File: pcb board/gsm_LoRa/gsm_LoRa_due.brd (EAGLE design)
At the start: 71.4 x 51.2 mm, 42 parts, among them IC1 TPS22810TDBVRQ1, IC2 TPS22810TDBVRQ1, IC3 DS3231MZ+, X1 22-23-2021

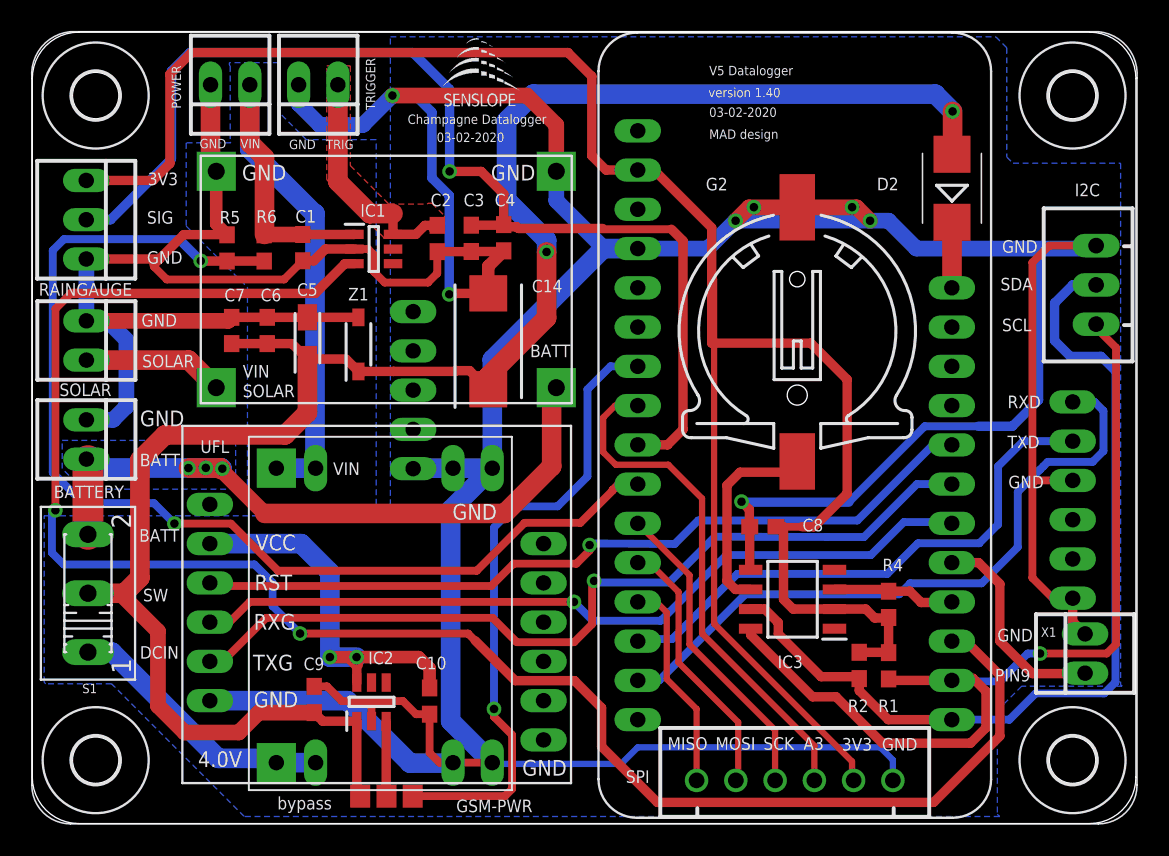
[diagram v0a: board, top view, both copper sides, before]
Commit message: updated traces and polygon
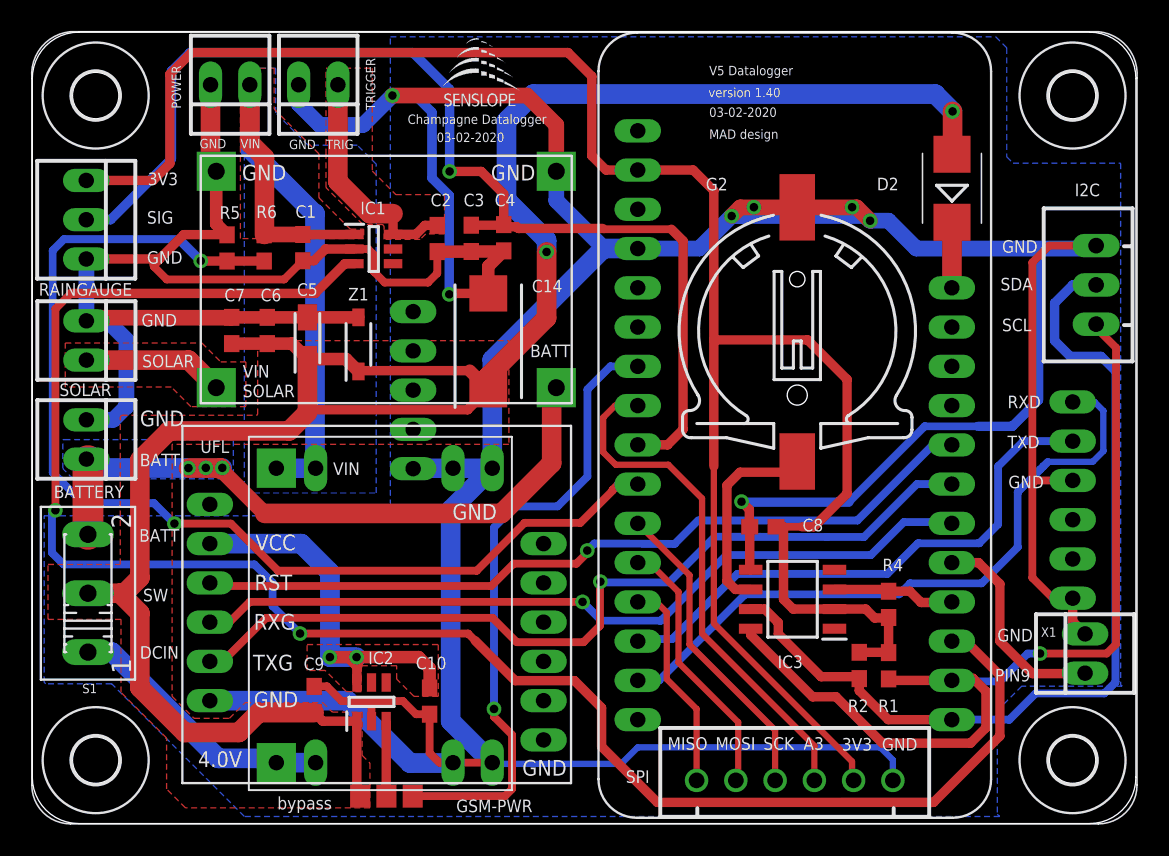
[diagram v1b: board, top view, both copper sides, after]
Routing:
- net 4V4: track 127.3 -> 139.6 mm
- net +3V3: track 138.1 -> 135.3 mm
- net GND: track 356.9 -> 357.6 mm
- added copper zone on layer 1, net 12VIN
- added copper zone on layer 1, net 4V4
- added copper zone on layer 1, net GSMPWR
- added copper zone on layer 1, net SOLAR

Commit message: addded ring pin to A0
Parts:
- C1, C10, C2, C3, C8, C9: value (none) -> 1uF
- C4: value (none) -> 100nF
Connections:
- removed net RTCVIN: U$1.P$5
- new net RING: U$1.P$5, U$9.RING
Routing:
- net RING: track 0.00 -> 25.5 mm, vias 0 -> 1
- net GSM_PSW: track 40.9 -> 39.3 mm
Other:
- board text added: "version 1.50"
- board text removed: "version 1.40"
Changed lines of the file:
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@@
 <grid distance="2" unitdist="mil" unit="mil" style="lines" multiple="1" display="yes" altdistance="1" altunitdist="mil" altunit="mil"/>
 <layers>
-<layer number="1" name="Top" color="4" fill="1" visible="yes" active="yes"/>
-<layer number="16" name="Bottom" color="1" fill="1" visible="yes" active="yes"/>
+<layer number="1" name="Top" color="4" fill="1" visible="no" active="yes"/>
+<layer number="16" name="Bottom" color="1" fill="1" visible="no" active="yes"/>
 <layer number="17" name="Pads" color="2" fill="1" visible="yes" active="yes"/>
 <layer number="18" name="Vias" color="2" fill="1" visible="yes" active="yes"/>
@@
 <text x="6.9596" y="10.5664" size="0.8128" layer="25">DCIN</text>
 <text x="7.1628" y="14.2748" size="0.8128" layer="25">SW</text>
-<text x="43.7388" y="46.8884" size="0.6096" layer="25">version 1.40</text>
+<text x="43.7388" y="46.8884" size="0.6096" layer="25">version 1.50</text>
 <text x="43.7896" y="48.3108" size="0.6096" layer="25">V5 Datalogger</text>
 <text x="43.7896" y="45.6184" size="0.6096" layer="25">03-02-2020</text>
@@
 </autorouter>
 <elements>
-<element name="C1" library="eagle-ltspice" library_urn="urn:adsk.eagle:library:217" package="C0603" package3d_urn="urn:adsk.eagle:package:13262/1" value="" x="17.5" y="37.16" smashed="yes" rot="R90">
+<element name="C1" library="eagle-ltspice" library_urn="urn:adsk.eagle:library:217" package="C0603" package3d_urn="urn:adsk.eagle:package:13262/1" value="1uF" x="17.5" y="37.16" smashed="yes" rot="R90">
 <attribute name="NAME" x="17.0218" y="39.0874" size="0.8128" layer="25"/>
 <attribute name="SPICEMODEL" value="NONE" x="144.5" y="90.5" size="1.778" layer="27" rot="R90" display="off"/>
@@
 <attribute name="VALUE" x="19.405" y="36.525" size="1.27" layer="27" rot="R90"/>
 </element>
-<element name="C2" library="eagle-ltspice" library_urn="urn:adsk.eagle:library:217" package="C0603" package3d_urn="urn:adsk.eagle:package:13262/1" value="" x="26.2" y="37.75" smashed="yes" rot="R270">
+<element name="C2" library="eagle-ltspice" library_urn="urn:adsk.eagle:library:217" package="C0603" package3d_urn="urn:adsk.eagle:package:13262/1" value="1uF" x="26.2" y="37.75" smashed="yes" rot="R270">
 <attribute name="NAME" x="25.769" y="39.835" size="0.8128" layer="25"/>
 <attribute name="SPICEMODEL" value="NONE" x="-100.8" y="-19.4" size="1.778" layer="27" rot="R270" display="off"/>
@@
 <attribute name="VALUE" x="24.295" y="38.385" size="1.27" layer="27" rot="R270"/>
 </element>
-<element name="C3" library="eagle-ltspice" library_urn="urn:adsk.eagle:library:217" package="C0603" package3d_urn="urn:adsk.eagle:package:13262/1" value="" x="28.4" y="37.76" smashed="yes" rot="R270">
+<element name="C3" library="eagle-ltspice" library_urn="urn:adsk.eagle:library:217" package="C0603" package3d_urn="urn:adsk.eagle:package:13262/1" value="1uF" x="28.4" y="37.76" smashed="yes" rot="R270">
 <attribute name="NAME" x="27.905" y="39.835" size="0.8128" layer="25"/>
 <attribute name="SPICEMODEL" value="NONE" x="-98.6" y="-23.2" size="1.778" layer="27" rot="R270" display="off"/>
@@
 <attribute name="POPULARITY" value="3" x="4.1" y="47" size="1.778" layer="27" display="off"/>
 </element>
-<element name="C4" library="eagle-ltspice" library_urn="urn:adsk.eagle:library:217" package="C0603" package3d_urn="urn:adsk.eagle:package:13262/1" value="" x="30.5" y="37.8" smashed="yes" rot="R270">
+<element name="C4" library="eagle-ltspice" library_urn="urn:adsk.eagle:library:217" package="C0603" package3d_urn="urn:adsk.eagle:package:13262/1" value="100nF" x="30.5" y="37.8" smashed="yes" rot="R270">
 <attribute name="NAME" x="29.9126" y="39.835" size="0.8128" layer="25"/>
 <attribute name="SPICEMODEL" value="NONE" x="30.5" y="37.8" size="1.778" layer="27" rot="R270" display="off"/>
@@
 <attribute name="VALUE" x="-1.58" y="27.2892" size="1.016" layer="27" ratio="10" rot="R270"/>
 </element>
-<element name="C8" library="eagle-ltspice" library_urn="urn:adsk.eagle:library:217" package="C0603" package3d_urn="urn:adsk.eagle:package:13262/1" value="" x="47.2652" y="19.1" smashed="yes">
+<element name="C8" library="eagle-ltspice" library_urn="urn:adsk.eagle:library:217" package="C0603" package3d_urn="urn:adsk.eagle:package:13262/1" value="1uF" x="47.2652" y="19.1" smashed="yes">
 <attribute name="NAME" x="49.829" y="18.8046" size="0.8128" layer="25"/>
 <attribute name="SPICEMODEL" value="NONE" x="47.2652" y="19.1" size="1.778" layer="27" display="off"/>
@@
 <attribute name="VALUE" x="21.9456" y="7.7724" size="1.27" layer="27" rot="R90" align="center"/>
 </element>
-<element name="C9" library="eagle-ltspice" library_urn="urn:adsk.eagle:library:217" package="C0603" package3d_urn="urn:adsk.eagle:package:13262/1" value="" x="18.2372" y="7.9248" smashed="yes" rot="R270">
+<element name="C9" library="eagle-ltspice" library_urn="urn:adsk.eagle:library:217" package="C0603" package3d_urn="urn:adsk.eagle:package:13262/1" value="1uF" x="18.2372" y="7.9248" smashed="yes" rot="R270">
 <attribute name="NAME" x="17.5514" y="9.8298" size="0.8128" layer="25"/>
 <attribute name="SPICEMODEL" value="NONE" x="18.2372" y="17.1704" size="1.778" layer="27" rot="R270" display="off"/>
@@
 <attribute name="VALUE" x="16.3322" y="8.5598" size="1.27" layer="27" rot="R270"/>
 </element>
-<element name="C10" library="eagle-ltspice" library_urn="urn:adsk.eagle:library:217" package="C0603" package3d_urn="urn:adsk.eagle:package:13262/1" value="" x="25.7048" y="7.8232" smashed="yes" rot="R270">
+<element name="C10" library="eagle-ltspice" library_urn="urn:adsk.eagle:library:217" package="C0603" package3d_urn="urn:adsk.eagle:package:13262/1" value="1uF" x="25.7048" y="7.8232" smashed="yes" rot="R270">
 <attribute name="NAME" x="24.8158" y="9.8806" size="0.8128" layer="25"/>
 <attribute name="SPICEMODEL" value="NONE" x="22.1996" y="12.9032" size="1.778" layer="27" rot="R270" display="off"/>
@@
 <wire x1="15.9004" y1="16.256" x2="12.8524" y2="19.304" width="0.508" layer="1"/>
 <wire x1="9.1948" y1="19.304" x2="12.8524" y2="19.304" width="0.508" layer="1"/>
-<wire x1="31.8516" y1="19.3548" x2="35.4584" y2="19.3548" width="0.508" layer="1"/>
-<wire x1="35.4584" y1="19.3548" x2="37.5412" y2="21.4376" width="0.508" layer="1"/>
-<wire x1="37.5412" y1="21.4376" x2="37.5412" y2="21.4884" width="0.508" layer="1"/>
-<wire x1="37.5412" y1="21.4884" x2="37.9128" y2="21.86" width="0.508" layer="1"/>
+<wire x1="33.5788" y1="21.082" x2="37.1348" y2="21.082" width="0.508" layer="1"/>
+<wire x1="37.1348" y1="21.082" x2="37.9128" y2="21.86" width="0.508" layer="1"/>
 <wire x1="37.9128" y1="21.86" x2="39.17" y2="21.86" width="0.508" layer="1"/>
 <wire x1="3.302" y1="20.6248" x2="7.874" y2="20.6248" width="0.508" layer="16"/>
 <wire x1="7.874" y1="20.6248" x2="9.1948" y2="19.304" width="0.508" layer="16"/>
-<wire x1="28.7528" y1="16.256" x2="31.8516" y2="19.3548" width="0.508" layer="1"/>
+<wire x1="28.7528" y1="16.256" x2="33.5788" y2="21.082" width="0.508" layer="1"/>
 </signal>
 <signal name="RAIN">
@@
 <wire x1="56.0832" y1="14.732" x2="46.1264" y2="14.732" width="0.508" layer="16"/>
 <wire x1="46.1264" y1="14.732" x2="40.5544" y2="9.16" width="0.508" layer="16"/>
-</signal>
-<signal name="RTCVIN">
-<contactref element="U$1" pad="P$5"/>
 </signal>
 <signal name="DUETRIG">
@@
 <contactref element="U$9" pad="RST"/>
 <contactref element="U$1" pad="P$24"/>
-<wire x1="35.904" y1="17.5624" x2="35.9788" y2="17.4876" width="0.508" layer="1"/>
+<wire x1="35.904" y1="17.5624" x2="35.9788" y2="17.4876" width="0.3048" layer="1"/>
 <wire x1="35.9788" y1="17.4876" x2="35.2044" y2="16.7132" width="0.508" layer="1"/>
 <wire x1="35.2044" y1="16.7132" x2="31.1404" y2="16.7132" width="0.508" layer="1"/>
@@
 <contactref element="GSM-PWR" pad="3"/>
 <wire x1="39.17" y1="29.48" x2="37.4048" y2="29.48" width="0.508" layer="16"/>
-<wire x1="35.9156" y1="27.9908" x2="35.9156" y2="22.352" width="0.508" layer="16"/>
-<wire x1="35.9156" y1="22.352" x2="33.9852" y2="20.4216" width="0.508" layer="16"/>
+<wire x1="35.9156" y1="27.9908" x2="35.9156" y2="25.0952" width="0.508" layer="16"/>
+<wire x1="35.9156" y1="25.0952" x2="29.8704" y2="19.05" width="0.508" layer="16"/>
 <wire x1="29.8704" y1="19.05" x2="29.8704" y2="7.3152" width="0.508" layer="16"/>
 <via x="29.8704" y="7.3152" extent="1-16" drill="0.55"/>
@@
 <wire x1="31.0388" y1="5.6388" x2="29.8704" y2="6.8072" width="0.508" layer="1"/>
 <wire x1="37.4048" y1="29.48" x2="35.9156" y2="27.9908" width="0.508" layer="16"/>
-<wire x1="33.9852" y1="20.4216" x2="31.242" y2="20.4216" width="0.508" layer="16"/>
-<wire x1="31.242" y1="20.4216" x2="29.8704" y2="19.05" width="0.508" layer="16"/>
 <wire x1="24.6108" y1="1.6764" x2="30.5816" y2="1.6764" width="0.508" layer="1"/>
 <wire x1="30.5816" y1="1.6764" x2="31.0388" y2="2.1336" width="0.508" layer="1"/>
 <wire x1="31.0388" y1="2.1336" x2="31.0388" y2="5.6388" width="0.508" layer="1"/>
 </signal>
+<signal name="RING">
+<contactref element="U$9" pad="RING"/>
+<contactref element="U$1" pad="P$5"/>
+<wire x1="33.076" y1="18.01" x2="34.6748" y2="19.6088" width="0.508" layer="1"/>
+<wire x1="34.6748" y1="19.6088" x2="35.814" y2="19.6088" width="0.508" layer="1"/>
+<via x="35.814" y="19.6088" extent="1-16" drill="0.5" diameter="0.95"/>
+<wire x1="35.814" y1="19.6088" x2="36.7792" y2="20.574" width="0.508" layer="16"/>
+<wire x1="40.8432" y1="20.574" x2="41.9608" y2="21.6916" width="0.508" layer="16"/>
+<wire x1="41.9608" y1="21.6916" x2="41.9608" y2="33.4772" width="0.508" layer="16"/>
+<wire x1="41.9608" y1="33.4772" x2="40.8432" y2="34.5948" width="0.508" layer="16"/>
+<wire x1="40.8432" y1="34.5948" x2="39.2048" y2="34.5948" width="0.508" layer="16"/>
+<wire x1="39.2048" y1="34.5948" x2="39.17" y2="34.56" width="0.508" layer="16"/>
+<wire x1="36.7792" y1="20.574" x2="40.8432" y2="20.574" width="0.508" layer="16"/>
+</signal>
 </signals>
